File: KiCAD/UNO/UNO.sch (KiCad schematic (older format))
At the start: 13 parts, among them P1 Power, P2 Analog, P3 Digital, P4 Digital

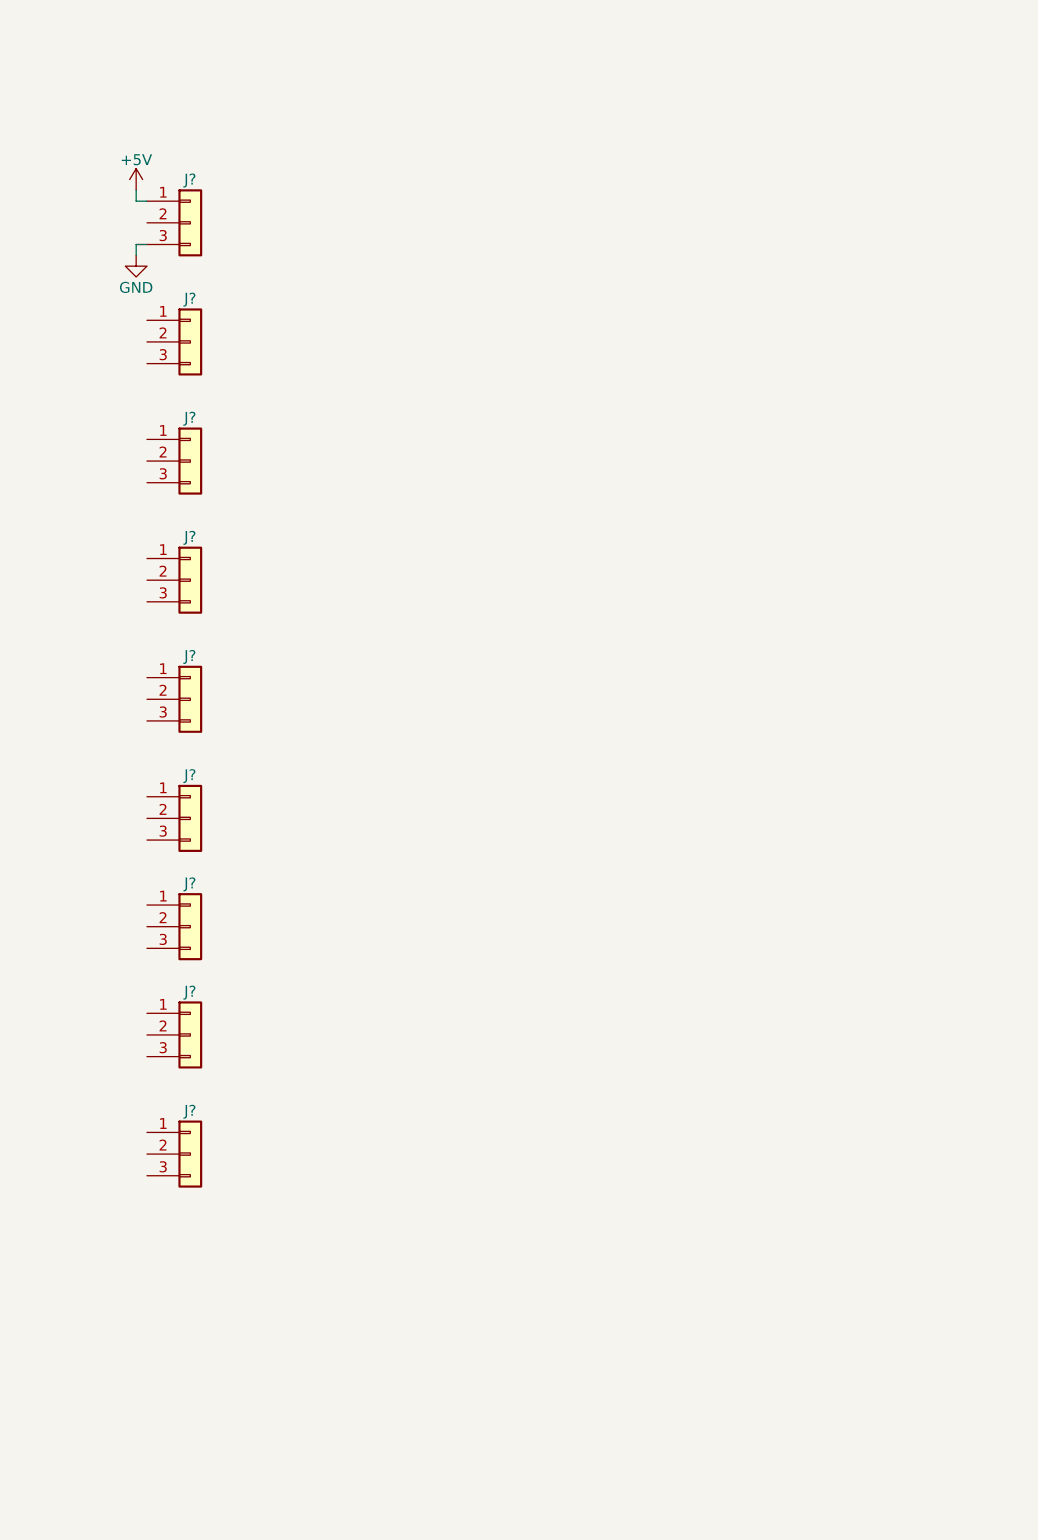
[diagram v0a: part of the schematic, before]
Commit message: 9 LEDs Added and Motor Connector
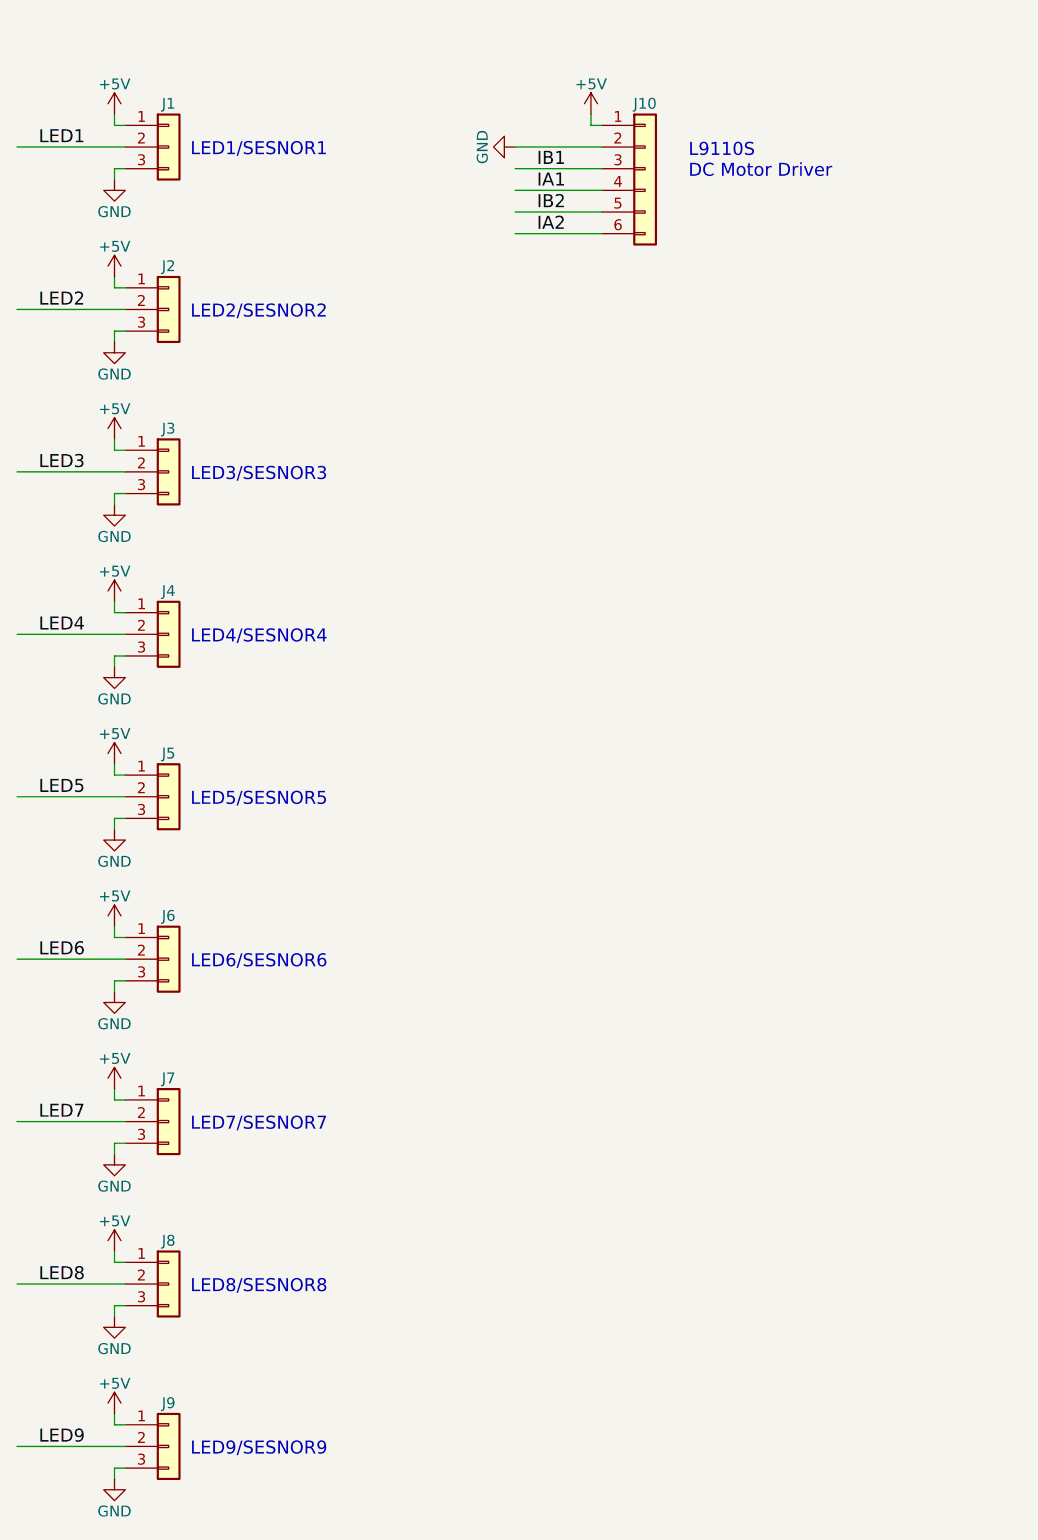
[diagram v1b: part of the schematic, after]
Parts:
- removed J? (x8): Conn_01x03, symbol Conn_01x03
- added J10: Conn_01x06, Socket_Strips:Socket_Strip_Straight_1x06_Pitch2.54mm, symbol Conn_01x06
- added J2, J3, J4, J5, J6, J7, J8, J9: Conn_01x03, Socket_Strips:Socket_Strip_Angled_1x03_Pitch2.54mm, symbol Conn_01x03
- J1: renamed from J?; footprint (none) -> Socket_Strips:Socket_Strip_Angled_1x03_Pitch2.54mm
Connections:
- net labels added: IA1, IA2, IB1, IB2, LED1, LED2, LED3, LED4, LED5, LED6, LED7, LED8, LED9
- wire segments 41 -> 89
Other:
- note added: "L9110S\nDC Motor Driver"
- note added: "LED1/SESNOR1"
- note added: "LED2/SESNOR2"
- note added: "LED3/SESNOR3"
- note added: "LED4/SESNOR4"
- note added: "LED5/SESNOR5"
- note added: "LED6/SESNOR6"
- note added: "LED7/SESNOR7"
- note added: "LED8/SESNOR8"
- note added: "LED9/SESNOR9"
- moved on the sheet: J1

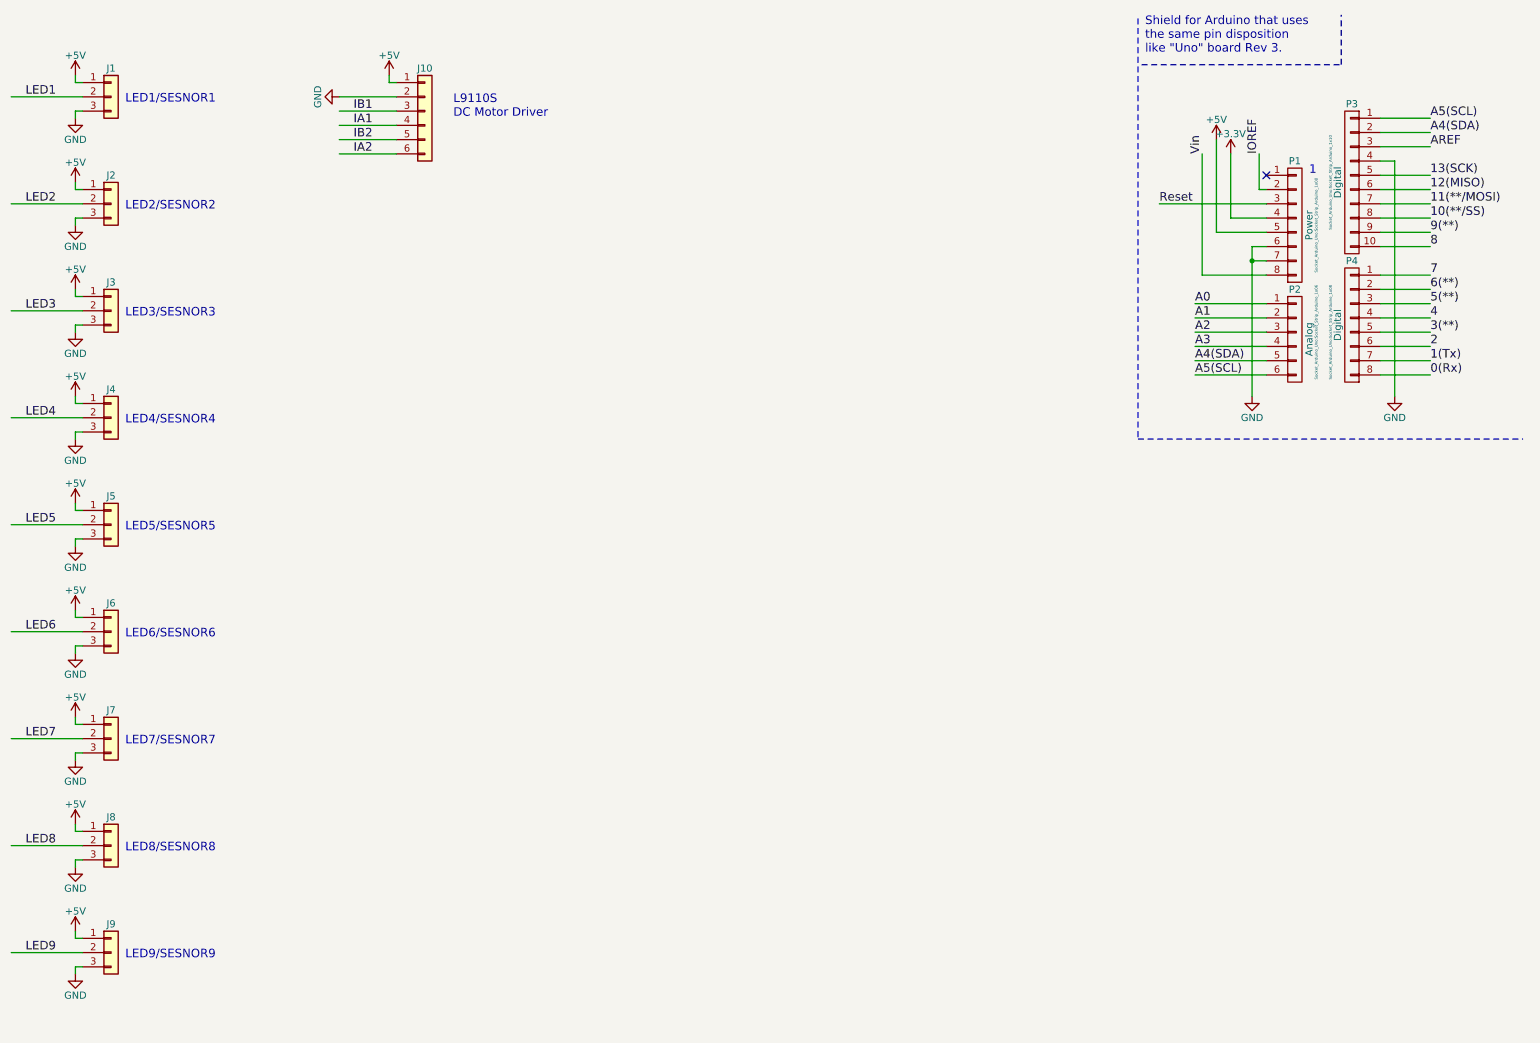
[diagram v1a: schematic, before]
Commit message: More connctors added
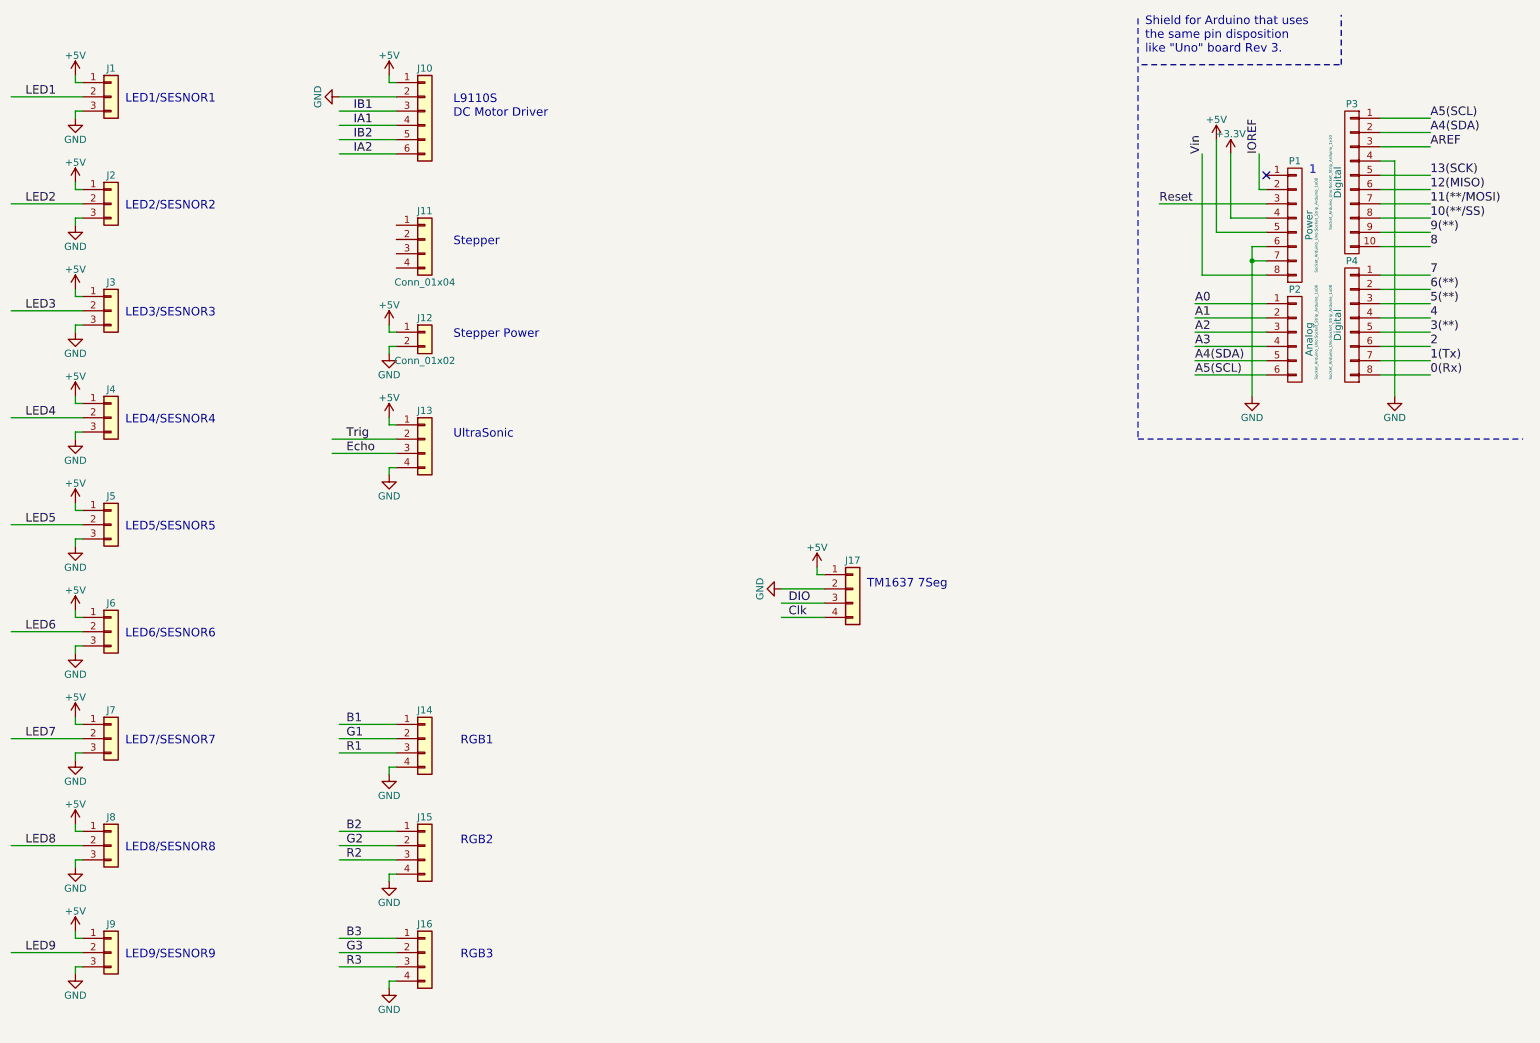
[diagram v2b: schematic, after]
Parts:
- added J11, J13: Conn_01x04, Socket_Strips:Socket_Strip_Straight_1x04_Pitch2.54mm, symbol Conn_01x04
- added J12: Conn_01x02, Socket_Strips:Socket_Strip_Straight_1x02_Pitch2.54mm, symbol Conn_01x02
- added J14, J15, J16, J17: Conn_01x04, Socket_Strips:Socket_Strip_Angled_1x04_Pitch2.54mm, symbol Conn_01x04
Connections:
- net labels added: B1, B2, B3, Clk, DIO, Echo, G1, G2, G3, R1, R2, R3, Trig
- wire segments 89 -> 119
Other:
- note added: "RGB1"
- note added: "RGB2"
- note added: "RGB3"
- note added: "Stepper"
- note added: "Stepper Power"
- note added: "TM1637 7Seg"
- note added: "UltraSonic"

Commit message: no message
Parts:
- removed J1, J2, J3, J4, J5, J6, J7, J8, J9: Conn_01x03, Socket_Strips:Socket_Strip_Angled_1x03_Pitch2.54mm, symbol Conn_01x03
- added J1, J2, J3, J4, J5, J6, J7, J8, J9: Conn_01x04, Socket_Strips:Socket_Strip_Angled_1x04_Pitch2.54mm, symbol Conn_01x04
- added J18, J19, J20, J21, J22, J23, J24, J25, J26: Conn_01x02, Pin_Headers:Pin_Header_Straight_1x02_Pitch2.54mm, symbol Conn_01x02
- added R1, R11, R13, R15, R17, R3, R5, R7, R9: R, Resistors_SMD:R_0603_HandSoldering, symbol R
- added R10, R12, R14, R16, R18, R2, R4, R6, R8: R, Resistors_THT:R_Axial_DIN0204_L3.6mm_D1.6mm_P5.08mm_Horizontal, symbol R
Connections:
- net labels removed: LED2, LED3, LED4, LED5, LED6, LED7, LED8, LED9
- wire segments 119 -> 200
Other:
- moved on the sheet: J10, J11, J12, J13, J14, J15, J16
